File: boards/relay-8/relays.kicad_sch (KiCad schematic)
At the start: 56 parts, among them J10 Screw_Terminal_01x02, J11 Screw_Terminal_01x02, J4 Screw_Terminal_01x02, J5 Screw_Terminal_01x02, J6 Screw_Terminal_01x02, J7 Screw_Terminal_01x02, J8 Screw_Terminal_01x02, J9 Screw_Terminal_01x02, K1 RT42xxxx, K2 RT42xxxx, K3 RT42xxxx, K4 RT42xxxx, K5 RT42xxxx, K6 RT42xxxx, K7 RT42xxxx, K8 RT42xxxx, Q1 BC847, Q2 BC847, Q3 BC847, Q4 BC847, Q5 BC847, Q6 BC847, Q7 BC847, Q8 BC847

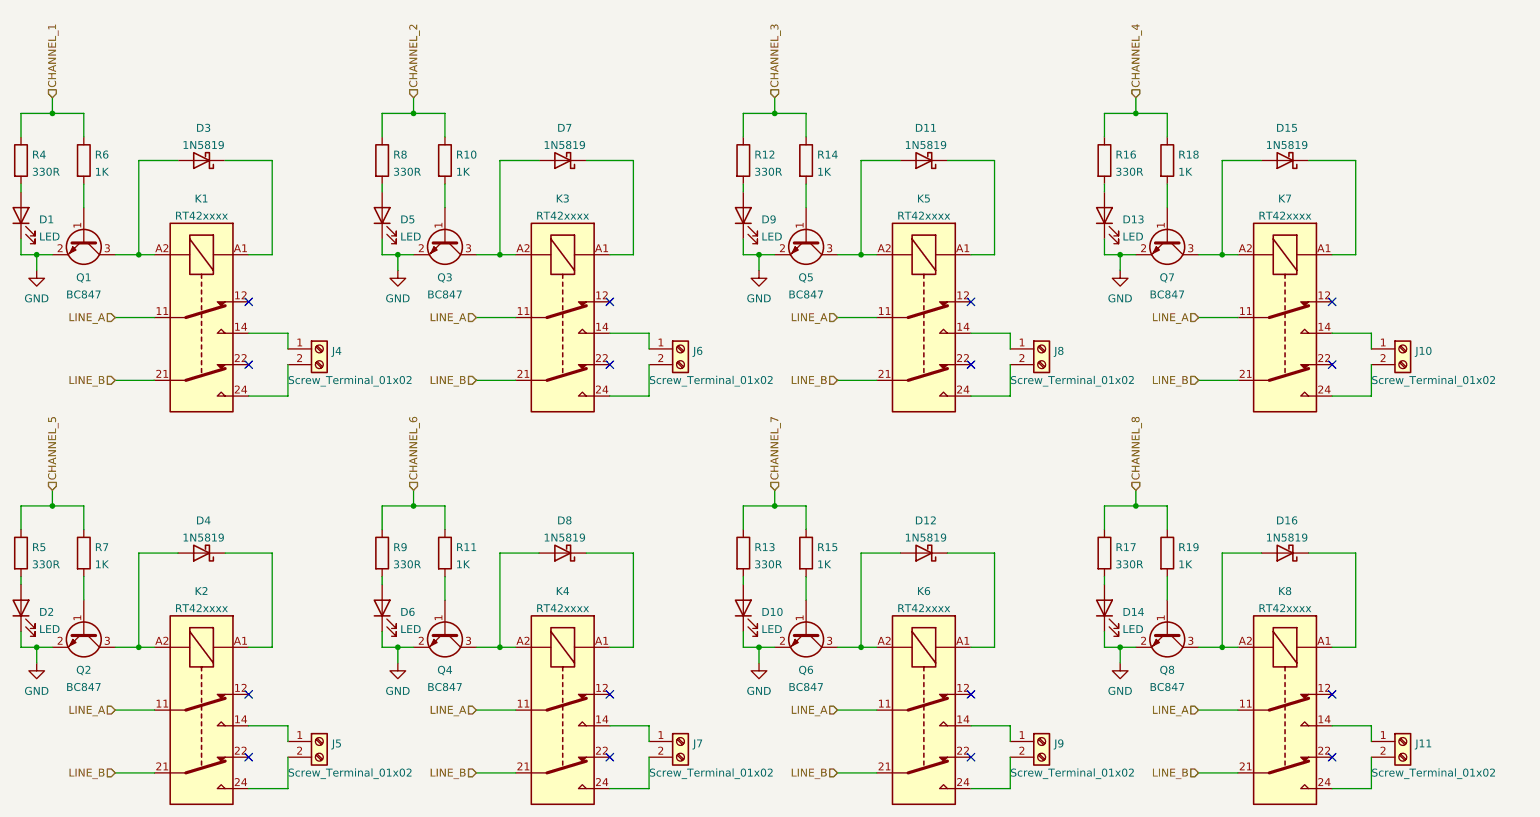
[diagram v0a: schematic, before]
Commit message: Added 12V for relays
Signed-off-by: Computroniks <mnickson@sidingsmedia.com>
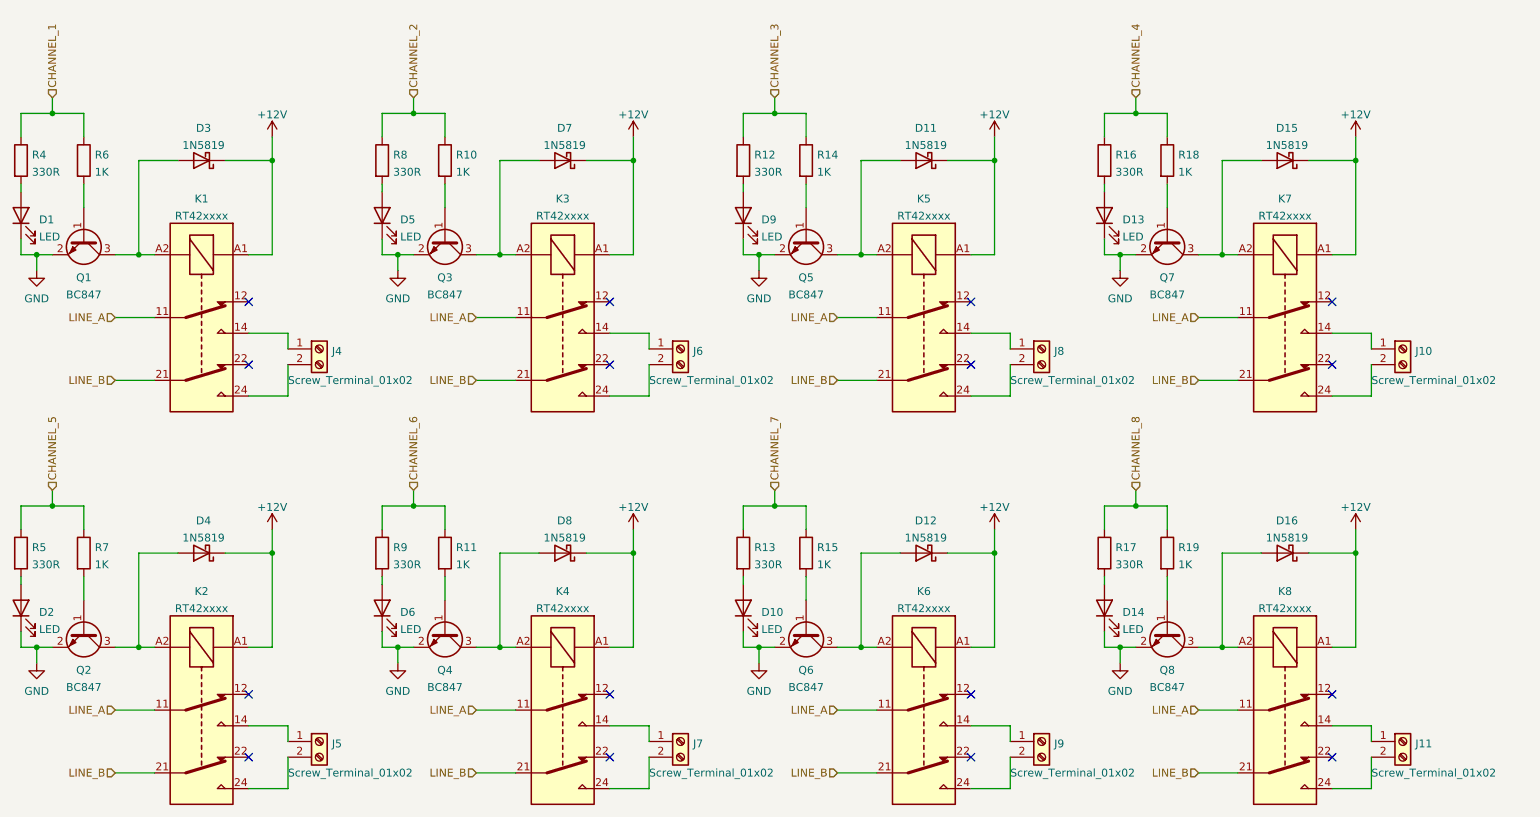
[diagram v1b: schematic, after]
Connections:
- net +12V: now reaches D3.1 (K), K1.A1
- net +12V: now also D11.1 (K), D12.1 (K), D15.1 (K), D16.1 (K), D4.1 (K), D7.1 (K), D8.1 (K), K2.A1, K3.A1, K4.A1, K5.A1, K6.A1, K7.A1, K8.A1
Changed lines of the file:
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@@
   (title_block
     (title "8 Channel Relay")
-    (date "2022-03-19")
-    (rev "1.0.0")
+    (date "2022-03-20")
+    (rev "1.0.1")
     (company "Matthew Nickson")
     (comment 1 "Licence: CC-BY-SA-4.0")
@@
   (junction (at 93.98 50.8) (diameter 0) (color 0 0 0 0)
   )
+  (junction (at 173.99 35.56) (diameter 0) (color 0 0 0 0)
+  )
+  (junction (at 57.15 35.56) (diameter 0) (color 0 0 0 0)
+  )
   (junction (at 77.47 50.8) (diameter 0) (color 0 0 0 0)
   )
+  (junction (at 232.41 35.56) (diameter 0) (color 0 0 0 0)
+  )
   (junction (at 196.85 27.94) (diameter 0) (color 0 0 0 0)
   )
@@
   (junction (at 19.05 114.3) (diameter 0) (color 0 0 0 0)
   )
+  (junction (at 115.57 99.06) (diameter 0) (color 0 0 0 0)
+  )
   (junction (at 152.4 50.8) (diameter 0) (color 0 0 0 0)
   )
   (junction (at 138.43 91.44) (diameter 0) (color 0 0 0 0)
   )
+  (junction (at 232.41 99.06) (diameter 0) (color 0 0 0 0)
+  )
   (junction (at 135.89 50.8) (diameter 0) (color 0 0 0 0)
   )
@@
   (junction (at 21.59 27.94) (diameter 0) (color 0 0 0 0)
   )
+  (junction (at 115.57 35.56) (diameter 0) (color 0 0 0 0)
+  )
   (junction (at 138.43 27.94) (diameter 0) (color 0 0 0 0)
   )
@@
   (junction (at 21.59 91.44) (diameter 0) (color 0 0 0 0)
   )
+  (junction (at 57.15 99.06) (diameter 0) (color 0 0 0 0)
+  )
   (junction (at 196.85 91.44) (diameter 0) (color 0 0 0 0)
+  )
+  (junction (at 173.99 99.06) (diameter 0) (color 0 0 0 0)
   )
   (junction (at 80.01 27.94) (diameter 0) (color 0 0 0 0)
@@
     (stroke (width 0) (type default) (color 0 0 0 0))
   )
+  (wire (pts (xy 57.15 31.75) (xy 57.15 35.56))
+    (stroke (width 0) (type default) (color 0 0 0 0))
+  )
   (wire (pts (xy 133.35 50.8) (xy 135.89 50.8))
     (stroke (width 0) (type default) (color 0 0 0 0))
@@
     (stroke (width 0) (type default) (color 0 0 0 0))
   )
+  (wire (pts (xy 173.99 95.25) (xy 173.99 99.06))
+    (stroke (width 0) (type default) (color 0 0 0 0))
+  )
   (wire (pts (xy 74.93 114.3) (xy 77.47 114.3))
     (stroke (width 0) (type default) (color 0 0 0 0))
@@
     (stroke (width 0) (type default) (color 0 0 0 0))
   )
+  (wire (pts (xy 232.41 95.25) (xy 232.41 99.06))
+    (stroke (width 0) (type default) (color 0 0 0 0))
+  )
   (wire (pts (xy 133.35 48.26) (xy 133.35 50.8))
     (stroke (width 0) (type default) (color 0 0 0 0))
@@
     (stroke (width 0) (type default) (color 0 0 0 0))
   )
+  (wire (pts (xy 232.41 31.75) (xy 232.41 35.56))
+    (stroke (width 0) (type default) (color 0 0 0 0))
+  )
   (wire (pts (xy 232.41 50.8) (xy 228.6 50.8))
     (stroke (width 0) (type default) (color 0 0 0 0))
@@
     (stroke (width 0) (type default) (color 0 0 0 0))
   )
+  (wire (pts (xy 115.57 31.75) (xy 115.57 35.56))
+    (stroke (width 0) (type default) (color 0 0 0 0))
+  )
   (wire (pts (xy 111.76 127) (xy 118.11 127))
     (stroke (width 0) (type default) (color 0 0 0 0))
@@
     (stroke (width 0) (type default) (color 0 0 0 0))
   )
+  (wire (pts (xy 173.99 31.75) (xy 173.99 35.56))
+    (stroke (width 0) (type default) (color 0 0 0 0))
+  )
   (wire (pts (xy 210.82 35.56) (xy 210.82 50.8))
     (stroke (width 0) (type default) (color 0 0 0 0))
@@
     (stroke (width 0) (type default) (color 0 0 0 0))
   )
+  (wire (pts (xy 115.57 95.25) (xy 115.57 99.06))
+    (stroke (width 0) (type default) (color 0 0 0 0))
+  )
   (wire (pts (xy 228.6 127) (xy 234.95 127))
     (stroke (width 0) (type default) (color 0 0 0 0))
@@
   )
   (wire (pts (xy 35.56 50.8) (xy 38.1 50.8))
+    (stroke (width 0) (type default) (color 0 0 0 0))
+  )
+  (wire (pts (xy 57.15 95.25) (xy 57.15 99.06))
     (stroke (width 0) (type default) (color 0 0 0 0))
   )
@@
     (pin "2")
   )
+  (symbol (lib_id "power:+12V") (at 173.99 31.75 0) (unit 1)
+    (in_bom yes) (on_board yes) (fields_autoplaced)
+    (property "Reference" "#PWR?" (id 0) (at 173.99 35.56 0)
+      (effects (font (size 1.27 1.27)) hide)
+    )
+    (property "Value" "+12V" (id 1) (at 173.99 28.1455 0))
+    (property "Footprint" "" (id 2) (at 173.99 31.75 0)
+      (effects (font (size 1.27 1.27)) hide)
+    )
+    (property "Datasheet" "" (id 3) (at 173.99 31.75 0)
+      (effects (font (size 1.27 1.27)) hide)
+    )
+    (pin "1")
+  )
   (symbol (lib_id "Connector:Screw_Terminal_01x02") (at 64.77 129.54 0) (unit 1)
     (in_bom yes) (on_board yes)
@@
     (pin "1")
     (pin "2")
+  )
+  (symbol (lib_id "power:+12V") (at 173.99 95.25 0) (unit 1)
+    (in_bom yes) (on_board yes) (fields_autoplaced)
+    (property "Reference" "#PWR?" (id 0) (at 173.99 99.06 0)
+      (effects (font (size 1.27 1.27)) hide)
+    )
+    (property "Value" "+12V" (id 1) (at 173.99 91.6455 0))
+    (property "Footprint" "" (id 2) (at 173.99 95.25 0)
+      (effects (font (size 1.27 1.27)) hide)
+    )
+    (property "Datasheet" "" (id 3) (at 173.99 95.25 0)
+      (effects (font (size 1.27 1.27)) hide)
+    )
+    (pin "1")
   )
   (symbol (lib_id "Device:R") (at 133.35 99.06 0) (unit 1)
@@
     (pin "2")
   )
+  (symbol (lib_id "power:+12V") (at 115.57 95.25 0) (unit 1)
+    (in_bom yes) (on_board yes) (fields_autoplaced)
+    (property "Reference" "#PWR?" (id 0) (at 115.57 99.06 0)
+      (effects (font (size 1.27 1.27)) hide)
+    )
+    (property "Value" "+12V" (id 1) (at 115.57 91.6455 0))
+    (property "Footprint" "" (id 2) (at 115.57 95.25 0)
+      (effects (font (size 1.27 1.27)) hide)
+    )
+    (property "Datasheet" "" (id 3) (at 115.57 95.25 0)
+      (effects (font (size 1.27 1.27)) hide)
+    )
+    (pin "1")
+  )
   (symbol (lib_id "Diode:1N5819") (at 45.72 99.06 180) (unit 1)
     (in_bom yes) (on_board yes) (fields_autoplaced)
@@
     (pin "A2")
   )
+  (symbol (lib_id "power:+12V") (at 232.41 31.75 0) (unit 1)
+    (in_bom yes) (on_board yes) (fields_autoplaced)
+    (property "Reference" "#PWR?" (id 0) (at 232.41 35.56 0)
+      (effects (font (size 1.27 1.27)) hide)
+    )
+    (property "Value" "+12V" (id 1) (at 232.41 28.1455 0))
+    (property "Footprint" "" (id 2) (at 232.41 31.75 0)
+      (effects (font (size 1.27 1.27)) hide)
+    )
+    (property "Datasheet" "" (id 3) (at 232.41 31.75 0)
+      (effects (font (size 1.27 1.27)) hide)
+    )
+    (pin "1")
+  )
   (symbol (lib_id "Connector:Screw_Terminal_01x02") (at 123.19 66.04 0) (unit 1)
     (in_bom yes) (on_board yes)
@@
     (pin "1")
     (pin "2")
+  )
+  (symbol (lib_id "power:+12V") (at 232.41 95.25 0) (unit 1)
+    (in_bom yes) (on_board yes) (fields_autoplaced)
+    (property "Reference" "#PWR?" (id 0) (at 232.41 99.06 0)
+      (effects (font (size 1.27 1.27)) hide)
+    )
+    (property "Value" "+12V" (id 1) (at 232.41 91.6455 0))
+    (property "Footprint" "" (id 2) (at 232.41 95.25 0)
+      (effects (font (size 1.27 1.27)) hide)
+    )
+    (property "Datasheet" "" (id 3) (at 232.41 95.25 0)
+      (effects (font (size 1.27 1.27)) hide)
+    )
+    (pin "1")
   )
   (symbol (lib_id "Transistor_BJT:BC847") (at 143.51 48.26 270) (unit 1)
@@
     (pin "2")
   )
+  (symbol (lib_id "power:+12V") (at 115.57 31.75 0) (unit 1)
+    (in_bom yes) (on_board yes) (fields_autoplaced)
+    (property "Reference" "#PWR?" (id 0) (at 115.57 35.56 0)
+      (effects (font (size 1.27 1.27)) hide)
+    )
+    (property "Value" "+12V" (id 1) (at 115.57 28.1455 0))
+    (property "Footprint" "" (id 2) (at 115.57 31.75 0)
+      (effects (font (size 1.27 1.27)) hide)
+    )
+    (property "Datasheet" "" (id 3) (at 115.57 31.75 0)
+      (effects (font (size 1.27 1.27)) hide)
+    )
+    (pin "1")
+  )
   (symbol (lib_id "Transistor_BJT:BC847") (at 26.67 48.26 270) (unit 1)
     (in_bom yes) (on_board yes) (fields_autoplaced)
@@
     (pin "2")
   )
+  (symbol (lib_id "power:+12V") (at 57.15 95.25 0) (unit 1)
+    (in_bom yes) (on_board yes) (fields_autoplaced)
+    (property "Reference" "#PWR?" (id 0) (at 57.15 99.06 0)
+      (effects (font (size 1.27 1.27)) hide)
+    )
+    (property "Value" "+12V" (id 1) (at 57.15 91.6455 0))
+    (property "Footprint" "" (id 2) (at 57.15 95.25 0)
+      (effects (font (size 1.27 1.27)) hide)
+    )
+    (property "Datasheet" "" (id 3) (at 57.15 95.25 0)
+      (effects (font (size 1.27 1.27)) hide)
+    )
+    (pin "1")
+  )
   (symbol (lib_id "Relay:RT42xxxx") (at 220.98 60.96 270) (unit 1)
     (in_bom yes) (on_board yes) (fields_autoplaced)
@@
     (pin "2")
   )
+  (symbol (lib_id "power:+12V") (at 57.15 31.75 0) (unit 1)
+    (in_bom yes) (on_board yes) (fields_autoplaced)
+    (property "Reference" "#PWR?" (id 0) (at 57.15 35.56 0)
+      (effects (font (size 1.27 1.27)) hide)
+    )
+    (property "Value" "+12V" (id 1) (at 57.15 28.1455 0))
+    (property "Footprint" "" (id 2) (at 57.15 31.75 0)
+      (effects (font (size 1.27 1.27)) hide)
+    )
+    (property "Datasheet" "" (id 3) (at 57.15 31.75 0)
+      (effects (font (size 1.27 1.27)) hide)
+    )
+    (pin "1")
+  )
   (symbol (lib_id "Connector:Screw_Terminal_01x02") (at 64.77 66.04 0) (unit 1)
